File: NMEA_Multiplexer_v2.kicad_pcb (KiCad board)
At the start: 2 copper layers, 98 parts, among them J1 USB, J2 Port 1, J3 Port 2, J4 Port 3, J5 Port 4, J6 Port 5, J7 12V, J8 DEBUG UART, J9 JTAG, SW1 Reset, U1 ATSAMG55J19A-AU, U2 XR32330, U3 XR32330, U4 LF33ABDT-TR, U5 HM-11, Y1 32.768k

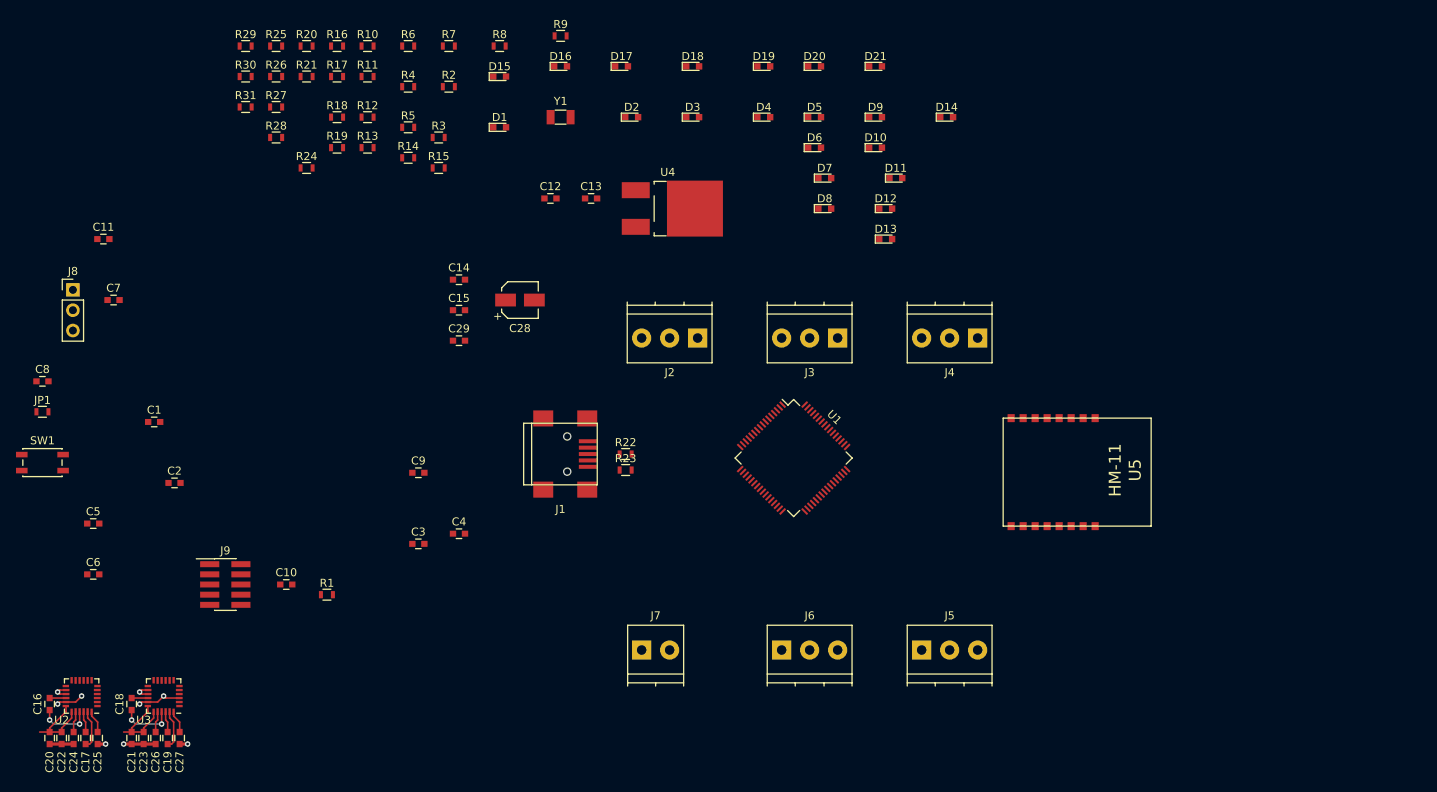
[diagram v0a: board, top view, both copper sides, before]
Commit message: Schematic ok Most of components placed on PCB
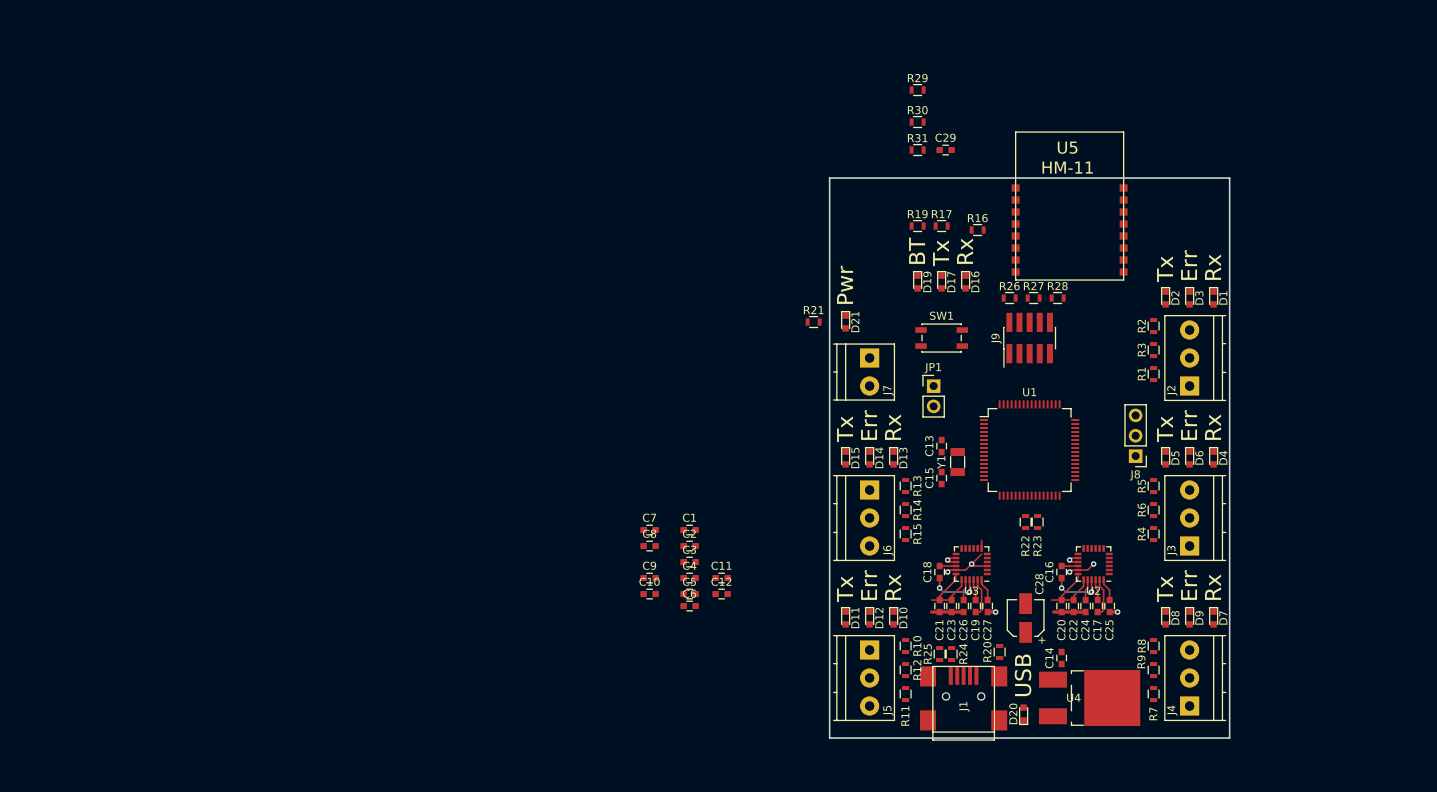
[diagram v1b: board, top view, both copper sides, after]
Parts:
- removed D18: Err BT (red), LEDs:LED_0603
- removed R18: 220, Resistors_SMD:R_0603
- JP1: footprint Resistors_SMD:R_0603 -> Pin_Headers:Pin_Header_Straight_1x02_Pitch2.54mm
- U2, U3: footprint MaxNil:QFN-24_4x4mm_Pitch0.5mm_NoMask -> Housings_DFN_QFN:QFN-24_4x4mm_Pitch0.5mm_NoMask
- moved J8 134.5 mm to (238.2, 114.8), turned to 180 degrees
- moved C16 127.6 mm to (229.0, 129.2)
- moved C17 127.6 mm to (233.5, 133.5)
- moved C20 127.6 mm to (229.0, 133.5)
- moved C22 127.6 mm to (230.5, 133.5)
- moved C24 127.6 mm to (232.0, 133.5)
- moved C25 127.6 mm to (235.0, 133.5)
- moved U2 127.6 mm to (233.0, 128.2)
- moved R7 119.7 mm to (240.5, 144.5), turned to 90 degrees
- moved R20 115.1 mm to (221.2, 139.2), turned to 270 degrees
- moved SW1 113.5 mm to (214.0, 100.0)
- moved R25 112.5 mm to (213.8, 139.5), turned to 90 degrees
- moved JP1 111.4 mm to (213.0, 106.0)
- moved R8 110.9 mm to (240.5, 138.5), turned to 90 degrees
- moved R6 109.8 mm to (240.5, 121.5), turned to 90 degrees
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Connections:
- J2 pad 2: /RX0 -> GND
- J2 pad 3: GND -> /RX0
- J3 pad 2: /RX1 -> GND
- J3 pad 3: GND -> /RX1
- J4 pad 2: /RX2 -> GND
- J4 pad 3: GND -> /RX2
- J5 pad 2: /RX3 -> GND
- J5 pad 3: GND -> /RX3
- J6 pad 2: /RX4 -> GND
- J6 pad 3: GND -> /RX4
- U1 pad 17: (no net) -> /TXD2
- U1 pad 61: /TDI -> /LED_0_ERR
- U1 pad 62: (no net) -> /TDI
- U1 pad 7: /TXD2 -> /LED_0_TX
- U3 pad 7: +3V3 -> GND
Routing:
- net GND: track 17.9 -> 21.4 mm, vias 7 -> 6
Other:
- board outline added: 50 x 70 mm
- rule via_min_drill: 0.3302 -> 0.254
- rule via_min_size: 0.6858 -> 0.508
- board text added: "BT"
- board text added: "Err"
- board text added: "Pwr"
- board text added: "Rx"
- board text added: "Tx"
- board text added: "USB"

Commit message: Before the renaming
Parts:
- moved J8 18.2 mm to (225.0, 127.2), turned to 0 degrees
- moved R28 12.0 mm to (220.2, 103.6), turned to 90 degrees
- moved R26 11.0 mm to (229.4, 103.6), turned to 270 degrees
- moved R27 6.34 mm to (229.4, 100.0), turned to 270 degrees
- moved C28 2.89 mm to (225.2, 137.8), turned to 180 degrees
- moved J9 1.81 mm to (224.8, 101.8), turned to 270 degrees
- moved R20 1.46 mm to (219.8, 139.4)
- moved C14 1.40 mm to (230.4, 140.0)
- moved C16 1.25 mm to (230.2, 129.2)
- moved C17 1.25 mm to (234.8, 133.5)
- moved C20 1.25 mm to (230.2, 133.5)
- moved C22 1.25 mm to (231.8, 133.5)
- moved C24 1.25 mm to (233.2, 133.5)
- moved C25 1.25 mm to (236.2, 133.5)
- moved U2 1.25 mm to (234.2, 128.2)
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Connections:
- net /LED_BT_ERR renamed Net-(U1-Pad57)
- net /TX4 renamed /TXX4
- J2 pad 1: /TX0 -> /TX2
- J2 pad 3: /RX0 -> /RX2
- J4 pad 1: /TX2 -> /TX0
- J4 pad 3: /RX2 -> /RX0
- U1 pad 17: /TXD2 -> /TXD4
- U1 pad 39: /RXD1 -> /RXD0
- U1 pad 40: /TXD1 -> /TXD0
- U1 pad 42: /TXD5 -> /TXD1
- U1 pad 43: /RXD5 -> /RXD1
- U1 pad 48: /TXD0 -> /TXD2
- U1 pad 49: /RXD0 -> /RXD2
- U1 pad 59: /TXD4 -> /TXD5
- U1 pad 60: /RXD4 -> /RXD5
- U1 pad 8: /RXD2 -> /RXD4
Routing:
- net GND: track 21.4 -> 113.2 mm, vias 6 -> 31
- net /RX2: track 0.00 -> 36.5 mm, vias 0 -> 1
- net /TX0: track 0.00 -> 30.7 mm
- net /TX2: track 0.00 -> 28.2 mm, vias 0 -> 2
- net /RX3: track 0.00 -> 25.7 mm, vias 0 -> 1
- net /TX3: track 0.00 -> 24.9 mm, vias 0 -> 1
- net /TXX4: track 0.00 -> 20.8 mm, vias 0 -> 1
- net /LED_3_TX: track 0.00 -> 19.7 mm
- net /RX4: track 0.00 -> 18.5 mm, vias 0 -> 1
- net /RX0: track 0.00 -> 17.7 mm, vias 0 -> 1
- net /RX1: track 0.00 -> 17.6 mm, vias 0 -> 1
- net /LED_3_ERR: track 0.00 -> 14.9 mm
- net /LED_3_RX: track 0.00 -> 13.0 mm
- net +3V3: track 24.2 -> 37.1 mm
- net Net-(D15-Pad2): track 0.00 -> 12.6 mm
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- added copper zone on B.Cu, net GND

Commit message: Placement complete
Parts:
- removed D20: USB Con (green), LEDs:LED_0603
- removed R20: 220, Resistors_SMD:R_0603
- moved C7 57.2 mm to (233.6, 113.0)
- moved C10 56.7 mm to (233.6, 124.0)
- moved C9 56.6 mm to (233.6, 122.8)
- moved C4 47.1 mm to (229.4, 126.0), turned to 270 degrees
- moved C5 43.7 mm to (225.8, 126.0), turned to 270 degrees
- moved C6 42.8 mm to (224.6, 126.0), turned to 270 degrees
- moved C12 42.1 mm to (228.2, 126.0), turned to 270 degrees
- moved C11 40.7 mm to (227.0, 126.0), turned to 270 degrees
- moved C8 38.5 mm to (214.0, 113.8), turned to 180 degrees
- moved C3 35.1 mm to (214.0, 112.6), turned to 180 degrees
- moved C2 34.7 mm to (214.0, 111.4), turned to 180 degrees
- moved C1 34.4 mm to (214.0, 110.2), turned to 180 degrees
- moved R29 26.2 mm to (211.6, 95.2), turned to 180 degrees
- moved R19 25.4 mm to (233.4, 98.0), turned to 180 degrees
- moved R7 23.6 mm to (233.6, 121.4), turned to 0 degrees
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- renumbered JP1 to ERA, J9 to JTAG
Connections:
- net /TXX4 renamed /TX4
- C10 pad 1: +3V3 -> +1V8
- C7 pad 1: +3V3 -> +1V8
- C8 pad 1: +3V3 -> +1V8
- C9 pad 1: +3V3 -> +1V8
- J8 pad 2: /TXD5 -> /TXD4
- J8 pad 3: /RXD5 -> /RXD4
- U1 pad 14: /LED_USB_CON -> /LED_4_RX
- U1 pad 15: Net-(U1-Pad15) -> /LED_4_ERR
- U1 pad 16: /RTS7 -> /LED_4_TX
- U1 pad 17: /TXD4 -> /TXD2
- U1 pad 18: Net-(U1-Pad18) -> /LED_3_RX
- U1 pad 19: /CTS7 -> /LED_3_ERR
- U1 pad 20: /LED_4_TX -> Net-(U1-Pad20)
- U1 pad 21: /TXD7 -> /LED_3_TX
- U1 pad 22: /LED_1_ERR -> /VBUS_3.3V
- U1 pad 23: /LED_2_ERR -> Net-(U1-Pad23)
- U1 pad 30: Net-(U1-Pad30) -> +1V8
- U1 pad 33: /BT_RESET_N -> /LED_2_RX
- U1 pad 34: /LED_2_RX -> /LED_2_ERR
- U1 pad 36: /VBUS_3.3V -> /LED_1_RX
- U1 pad 37: /LED_4_ERR -> /RXD6
- U1 pad 38: /LED_4_RX -> /TXD6
- U1 pad 39: /RXD0 -> /RXD1
- U1 pad 40: /TXD0 -> /TXD1
- U1 pad 41: /LED_1_TX -> /LED_1_ERR
- U1 pad 42: /TXD1 -> /TXD5
- U1 pad 43: /RXD1 -> /RXD5
- U1 pad 44: /LED_3_TX -> /LED_1_TX
- U1 pad 45: Net-(U1-Pad30) -> +1V8
- U1 pad 46: /LED_BT_RX -> /TXD4
- U1 pad 47: /LED_BT_TX -> /RXD4
- U1 pad 48: /TXD2 -> /TXD0
- U1 pad 49: /RXD2 -> /RXD0
- U1 pad 51: /RXD7 -> /BT_RESET_N
- U1 pad 52: /LED_3_ERR -> /RTS0
- U1 pad 56: /LED_1_RX -> /CTS0
- U1 pad 57: Net-(U1-Pad57) -> /LED_0_RX
- U1 pad 58: /LED_3_RX -> /LED_0_ERR
- U1 pad 59: /TXD5 -> /LED_0_TX
- U1 pad 6: /LED_0_RX -> Net-(U1-Pad6)
- U1 pad 60: /RXD5 -> /LED_BT_RX
- U1 pad 61: /LED_0_ERR -> /LED_BT_TX
- U1 pad 7: /LED_0_TX -> Net-(U1-Pad7)
- U1 pad 8: /RXD4 -> /RXD2
- U1 pad 9: Net-(U1-Pad30) -> +1V8
- U2 pad 10: /RXD2 -> /RXD5
- U2 pad 12: /RXD0 -> /RXD6
- U2 pad 7: /TXD2 -> /TXD5
- U2 pad 9: /TXD0 -> /TXD6
- U3 pad 11: /RXD4 -> /RXD2
- U3 pad 8: /TXD4 -> /TXD2
- U5 pad 1: /CTS7 -> /CTS0
- U5 pad 2: /RXD7 -> /RXD0
- U5 pad 3: /RTS7 -> /RTS0
- U5 pad 4: /TXD7 -> /TXD0
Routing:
- net GND: track 113.2 -> 65.0 mm, vias 31 -> 23
- net /RX2: track 36.5 -> 3.18 mm, vias 1 -> 0
- net /RX3: track 25.7 -> 0.00 mm, vias 1 -> 0
- net /TX3: track 24.9 -> 0.00 mm, vias 1 -> 0
- net /TX2: track 28.2 -> 3.62 mm, vias 2 -> 0
- net /TX4: track 20.8 -> 0.00 mm, vias 1 -> 0
- net /LED_3_TX: track 19.7 -> 0.00 mm
- net (no net): track 0.00 -> 19.4 mm, vias 0 -> 2
- net /RX4: track 18.5 -> 0.00 mm, vias 1 -> 0
- net /LED_3_ERR: track 14.9 -> 0.00 mm
- net /LED_3_RX: track 13.0 -> 0.00 mm
- net Net-(D15-Pad2): track 12.6 -> 0.00 mm
- net Net-(D11-Pad2): track 12.6 -> 0.00 mm
- net Net-(D1-Pad2): track 12.3 -> 0.00 mm
- net Net-(D7-Pad2): track 12.3 -> 0.00 mm
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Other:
- board size 50 x 70 mm -> 45 x 65 mm
- board text removed: "USB"

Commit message: Bottom half completed
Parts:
- removed ERA: ERASE, Pin_Headers:Pin_Header_Straight_1x02_Pitch2.54mm
- added JP1: ERASE, Pin_Headers:Pin_Header_Straight_1x02_Pitch2.00mm, F.Cu at (245.4, 121.6)
- D1: renamed from D11; value Tx 3 (green) -> Tx 3 (gReen)
- D11: renamed from D8; value Tx (green) -> Tx (gReen)
- D12: renamed from D9; value Err 2 (red) -> ERr 2 (reD)
- D14: renamed from D5; value Tx 1 (green) -> Tx 1 (gReen)
- D15: renamed from D6; value Err 1 (red) -> ERr 1 (reD)
- D17: renamed from D2; value Tx 0 (green) -> Tx 0 (gReen)
- D18: renamed from D3; value Err 0 (red) -> ERr 0 (reD)
- D2: renamed from D12; value Err 3 (red) -> ERr 3 (reD)
- D4: renamed from D14; value Tx 4 (green) -> Tx 4 (gReen)
- D5: renamed from D15; value Err 4 (red) -> ERr 4 (reD)
- D8: renamed from D19; value BT Con (blue) -> BT Cxon (blue)
- D9: renamed from D17; value Tx BT (green) -> Tx BT (gReen)
- J2: value Port 1 -> PoRt 1
- J3: value Port 2 -> PoRt 2
- J4: value Port 3 -> PoRt 3
- J5: value Port 4 -> PoRt 4
- J6: value Port 5 -> PoRt 5
- U2: renamed from U3; footprint Housings_DFN_QFN:QFN-24_4x4mm_Pitch0.5mm_NoMask -> MaxNil:QFN-24_4x4mm_Pitch0.5mm_NoMask
- U3: renamed from U2; footprint Housings_DFN_QFN:QFN-24_4x4mm_Pitch0.5mm_NoMask -> MaxNil:QFN-24_4x4mm_Pitch0.5mm_NoMask
- moved D19 61.3 mm to (260.6, 150.2), turned to 180 degrees
- moved D7 61.2 mm to (260.6, 109.2), turned to 180 degrees
- moved SW1 59.6 mm to (261.4, 113.6), turned to 180 degrees
- moved D18 59.4 mm to (260.6, 147.2), turned to 180 degrees
- moved U5 59.3 mm to (264.1, 133.9), turned to 270 degrees
- moved D17 57.7 mm to (260.6, 144.2), turned to 180 degrees
- moved D8 56.6 mm to (260.6, 117.6), turned to 180 degrees
- moved D9 55.4 mm to (260.6, 120.6), turned to 180 degrees
- moved D10 54.6 mm to (260.6, 123.6), turned to 180 degrees
- moved R9 49.8 mm to (256.0, 117.8), turned to 90 degrees
- moved J7 49.8 mm to (253.0, 112.2), turned to 180 degrees
- moved C13 46.8 mm to (254.6, 117.8), turned to 90 degrees
- moved R8 46.7 mm to (253.2, 117.8), turned to 270 degrees
- moved R29 45.8 mm to (251.0, 141.8), turned to 270 degrees
- moved J2 45.7 mm to (249.5, 147.2), turned to 0 degrees
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- renumbered C21 to C1, C3 to C10, C2 to C11, C1 to C12, C29 to C13, C28 to C14, C14 to C15, C20 to C16, C22 to C17, C24 to C18, C17 to C19, C23 to C2, C25 to C20, C16 to C21, C6 to C22, C11 to C23, C12 to C24, C9 to C25, C10 to C26, C4 to C27, C5 to C28, C7 to C29, C26 to C3, C19 to C4, C27 to C5, C18 to C6, C15 to C7, C13 to C8, C8 to C9, D16 to D10, D7 to D13, D4 to D16, D1 to D19, D10 to D3, D13 to D6, D21 to D7, JTAG to J9, R15 to R1, R19 to R10, R24 to R11, R25 to R12, R10 to R13, R11 to R14, R12 to R15, R22 to R16, R23 to R17, R9 to R18, R8 to R19, R14 to R2, R7 to R20, R6 to R21, R5 to R22, R4 to R23, R28 to R24, R27 to R25, R3 to R27, R1 to R28, R2 to R29, R13 to R3, R16 to R4, R17 to R5, R21 to R6, R31 to R7, R30 to R8, R29 to R9
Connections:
- net /CTS0 renamed /CxTS0
- net /LED_BT_CON renamed /LED_BT_CxON
- net /TCK renamed /TCxK
- D1 pad 2: Net-(D11-Pad2) -> Net-(D1-Pad2)
- D11 pad 2: Net-(D8-Pad2) (its old number) -> Net-(D11-Pad2)
- D12 pad 2: Net-(D9-Pad2) (its old number) -> Net-(D12-Pad2)
- D14 pad 2: Net-(D5-Pad2) -> Net-(D14-Pad2)
- D15 pad 2: Net-(D6-Pad2) (its old number) -> Net-(D15-Pad2)
- D16 pad 2: Net-(D4-Pad2) -> Net-(D16-Pad2)
- D17 pad 2: Net-(D2-Pad2) -> Net-(D17-Pad2)
- D18 pad 2: Net-(D3-Pad2) -> Net-(D18-Pad2)
- D19 pad 2: Net-(D1-Pad2) -> Net-(D19-Pad2)
- D2 pad 2: Net-(D12-Pad2) -> Net-(D2-Pad2)
- D3 pad 2: Net-(D10-Pad2) (its old number) -> Net-(D3-Pad2)
- D4 pad 2: Net-(D14-Pad2) -> Net-(D4-Pad2)
- D5 pad 2: Net-(D15-Pad2) -> Net-(D5-Pad2)
- R1 pad 1: /LED_4_ERR -> /LED_4_TX
- R1 pad 2: Net-(D15-Pad2) -> Net-(D4-Pad2)
- R13 pad 1: /LED_3_RX -> /LED_3_TX
- R13 pad 2: Net-(D10-Pad2) (its old number) -> Net-(D1-Pad2)
- R14 pad 1: /LED_3_TX -> /LED_3_ERR
- R14 pad 2: Net-(D11-Pad2) -> Net-(D2-Pad2)
- R15 pad 1: /LED_3_ERR -> /LED_3_RX
- R15 pad 2: Net-(D12-Pad2) -> Net-(D3-Pad2)
- R18 pad 1: /LED_2_ERR -> /LED_2_TX
- R18 pad 2: Net-(D9-Pad2) (its old number) -> Net-(D11-Pad2)
- R19 pad 1: /LED_2_TX -> /LED_2_ERR
- R19 pad 2: Net-(D8-Pad2) (its old number) -> Net-(D12-Pad2)
- R2 pad 1: /LED_4_TX -> /LED_4_ERR
- R2 pad 2: Net-(D14-Pad2) -> Net-(D5-Pad2)
- R21 pad 1: /LED_1_ERR -> /LED_1_RX
- R21 pad 2: Net-(D6-Pad2) (its old number) -> Net-(D16-Pad2)
- R22 pad 1: /LED_1_TX -> /LED_1_ERR
- R22 pad 2: Net-(D5-Pad2) -> Net-(D15-Pad2)
- R23 pad 1: /LED_1_RX -> /LED_1_TX
- R23 pad 2: Net-(D4-Pad2) -> Net-(D14-Pad2)
- R24 pad 2: /TDI -> /TMS
- R26 pad 2: /TMS -> /TDI
- R27 pad 1: /LED_0_ERR -> /LED_0_RX
- R27 pad 2: Net-(D3-Pad2) -> Net-(D19-Pad2)
- R28 pad 1: /LED_0_RX -> /LED_0_TX
- R28 pad 2: Net-(D1-Pad2) -> Net-(D17-Pad2)
- R29 pad 1: /LED_0_TX -> /LED_0_ERR
- R29 pad 2: Net-(D2-Pad2) -> Net-(D18-Pad2)
- U1 pad 18: /LED_3_RX -> /LED_3_TX
- U1 pad 20: Net-(U1-Pad20) -> /LED_3_RX
- U1 pad 21: /LED_3_TX -> Net-(U1-Pad21)
- U1 pad 33: /LED_2_RX -> /LED_2_TX
- U1 pad 35: /LED_2_TX -> /LED_2_RX
- U1 pad 60: /LED_BT_RX -> /LED_BT_TX
- U1 pad 61: /LED_BT_TX -> /LED_BT_RX
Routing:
- net GND: track 65.0 -> 124.8 mm, vias 23 -> 42
- net +3V3: track 32.0 -> 78.7 mm
- net /RX2: track 3.18 -> 38.5 mm, vias 0 -> 2
- net /TX2: track 3.62 -> 34.2 mm, vias 0 -> 2
- net /TXD0: track 0.00 -> 27.2 mm, vias 0 -> 2
- net /CxTS0: track 0.00 -> 26.9 mm, vias 0 -> 2
- net /RXD0: track 0.00 -> 26.4 mm, vias 0 -> 2
- net /LED_BT_CxON: track 0.00 -> 25.9 mm, vias 0 -> 2
- net /RTS0: track 0.00 -> 24.8 mm, vias 0 -> 2
- net /BT_RESET_N: track 0.00 -> 22.0 mm, vias 0 -> 2
- net /TCxK: track 0.00 -> 20.5 mm, vias 0 -> 2
- net Net-(D13-Pad2): track 0.00 -> 20.4 mm
- net Net-(J1-Pad2): track 0.00 -> 19.6 mm, vias 0 -> 2
- net Net-(J1-Pad3): track 0.00 -> 19.5 mm
- net (no net): track 19.4 -> 0.00 mm, vias 2 -> 0
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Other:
- board size 45 x 65 mm -> 65 x 45 mm
- board text added: "1"
- board text added: "2"
- board text added: "ERA"
- board text added: "G"
- board text added: "JTAG"
- board text added: "R"
- board text added: "T"

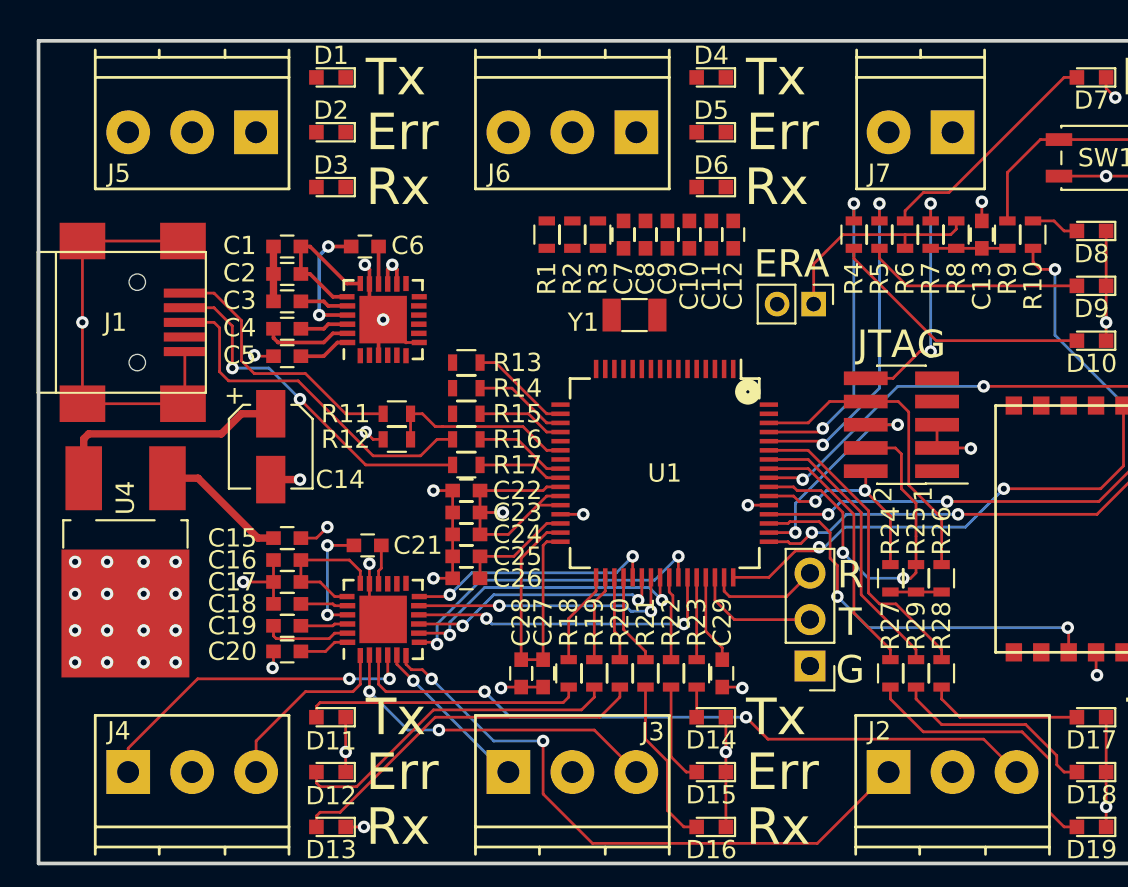
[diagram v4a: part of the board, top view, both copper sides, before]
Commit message: More connections
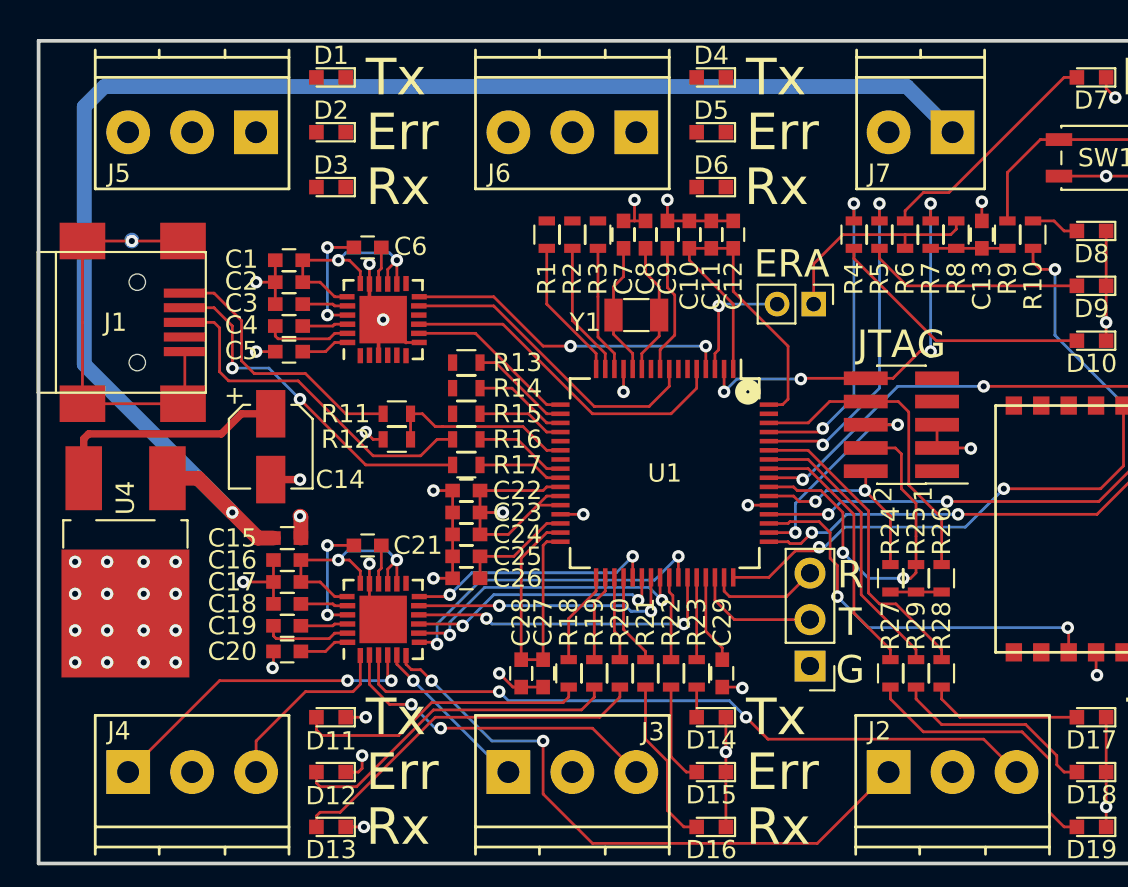
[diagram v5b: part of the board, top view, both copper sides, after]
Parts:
- moved C1 0.76 mm to (216.7, 119.2)
- moved C2 0.46 mm to (216.7, 120.4)
- moved C5 0.27 mm to (216.7, 124.2)
- moved C4 0.18 mm to (216.7, 122.8)
- moved C3 0.18 mm to (216.7, 121.6)
- moved C6 0.16 mm to (221.0, 118.5)
- moved Y1 0.10 mm to (235.7, 122.2)
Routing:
- net Net-(C15-Pad1): track 7.16 -> 81.7 mm, vias 0 -> 1
- net +3V3: track 78.7 -> 109.2 mm, vias 2 -> 5
- net /TXD3: track 0.00 -> 18.9 mm
- net /RXD3: track 0.00 -> 18.0 mm, vias 0 -> 2
- net /RXD2: track 0.00 -> 17.4 mm
- net /TXD2: track 0.00 -> 9.37 mm
- net /nRST: track 13.2 -> 22.5 mm, vias 2 -> 4
- net GND: track 124.8 -> 133.3 mm, vias 42 -> 47
- net /LED_4_TX: track 0.00 -> 7.72 mm
- net /LED_4_ERR: track 0.00 -> 7.35 mm
- net /XIN32: track 0.00 -> 7.30 mm
- net /XOUT32: track 0.00 -> 7.26 mm
- net +1V8: track 11.2 -> 18.3 mm
- net /LED_4_RX: track 0.00 -> 6.97 mm
- net Net-(JP1-Pad2): track 0.00 -> 6.77 mm, vias 0 -> 1
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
